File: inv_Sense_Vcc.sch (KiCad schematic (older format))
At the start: 7 parts, among them U1 ATtiny44-20SSU

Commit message: Rename to Sailor Hat
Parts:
- U1: symbol MCU_Microchip_ATtiny:ATtiny44-20SSU -> sailor-hat-rescue:ATtiny44-20SSU-MCU_Microchip_ATtiny
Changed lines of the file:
@@
-EESchema Schematic File Version 5
-LIBS:pi-supercap-ups-cache
+EESchema Schematic File Version 4
 EELAYER 30 0
 EELAYER END
@@
 Comment3 ""
 Comment4 ""
-Comment5 ""
-Comment6 ""
-Comment7 ""
-Comment8 ""
-Comment9 ""
 $EndDescr
 $Comp
@@
 	4850 2900 3800 2900
 $Comp
-L MCU_Microchip_ATtiny:ATtiny44-20SSU U1
+L sailor-hat-rescue:ATtiny44-20SSU-MCU_Microchip_ATtiny U1
 U 1 1 5D62E779
 P 3800 4500
+AR Path="/5D62E779" Ref="U1"  Part="1"
+AR Path="/5C33FF90/5D62E779" Ref="U1"  Part="1"
 F 0 "U1" H 3271 4546 50  0000 R CNN
 F 1 "ATtiny44-20SSU" H 3271 4455 50  0000 R CNN

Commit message: Update MCU to ATtiny841
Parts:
- U1: value ATtiny44-20SSU -> ATtiny841-SSU; symbol sailor-hat-rescue:ATtiny44-20SSU-MCU_Microchip_ATtiny -> MCU_Microchip_ATtiny:ATtiny841-SSU
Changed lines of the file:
@@
 	4850 2900 3800 2900
 $Comp
-L sailor-hat-rescue:ATtiny44-20SSU-MCU_Microchip_ATtiny U1
+L MCU_Microchip_ATtiny:ATtiny841-SSU U1
 U 1 1 5D62E779
 P 3800 4500
@@
 AR Path="/5C33FF90/5D62E779" Ref="U1"  Part="1"
 F 0 "U1" H 3271 4546 50  0000 R CNN
-F 1 "ATtiny44-20SSU" H 3271 4455 50  0000 R CNN
+F 1 "ATtiny841-SSU" H 3271 4455 50  0000 R CNN
 F 2 "Package_SO:SOIC-14_3.9x8.7mm_P1.27mm" H 3800 4500 50  0001 C CIN
 F 3 "http://ww1.microchip.com/downloads/en/DeviceDoc/doc8006.pdf" H 3800 4500 50  0001 C CNN

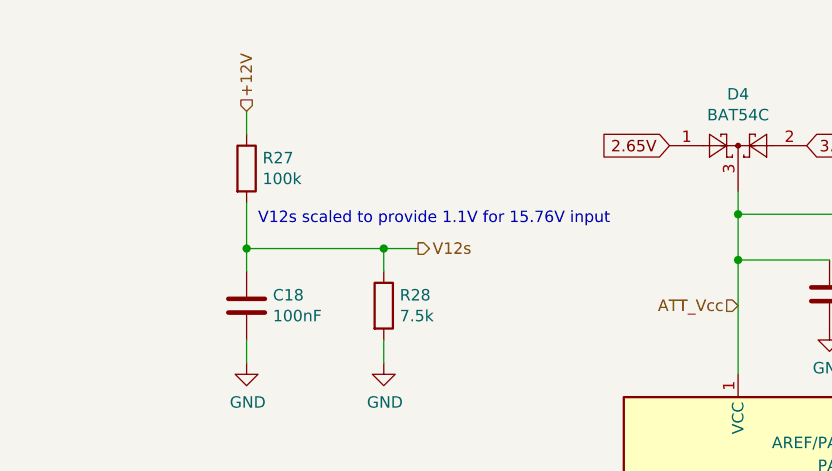
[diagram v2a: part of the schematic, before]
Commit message: Implement better current limiting
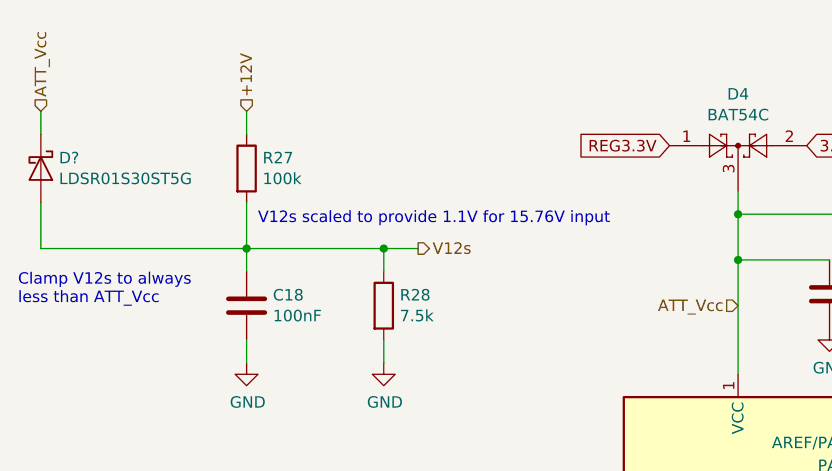
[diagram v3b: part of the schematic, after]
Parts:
- added D?: LDSR01S30ST5G, Diode_SMD:D_0603_1608Metric, symbol Device:D_Schottky
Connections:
- net ATT_Vcc: now also D?.1 (K)
- net V12s: now also D?.2 (A)
- net 2.65V renamed REG3.3V
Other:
- note added: "Clamp V12s to always\nless than ATT_Vcc"
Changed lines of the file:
@@
 $Descr A4 11693 8268
 encoding utf-8
-Sheet 4 7
+Sheet 4 6
 Title ""
 Date ""
@@
 $EndComp
 Text GLabel 3500 2600 0    50   Input ~ 0
-2.65V
+REG3.3V
 Wire Wire Line
 	5500 2900 4850 2900
@@
 Text Notes 1700 2950 0    50   ~ 0
 V12s scaled to provide 1.1V for 15.76V input
+Text HLabel 750  2450 1    50   Input ~ 0
+ATT_Vcc
+Wire Wire Line
+	750  2550 750  2450
+Wire Wire Line
+	750  2850 750  3050
+$Comp
+L Device:D_Schottky D?
+U 1 1 5E237065
+P 750 2700
+F 0 "D?" V 704 2779 50  0000 L CNN
+F 1 "LDSR01S30ST5G" V 795 2779 50  0000 L CNN
+F 2 "Diode_SMD:D_0603_1608Metric" H 750 2700 50  0001 C CNN
+F 3 "~" H 750 2700 50  0001 C CNN
+	1    750  2700
+	0    1    1    0
+$EndComp
+Wire Wire Line
+	750  3050 1650 3050
+Text Notes 650  3300 0    50   ~ 0
+Clamp V12s to always\nless than ATT_Vcc
 $EndSCHEMATC

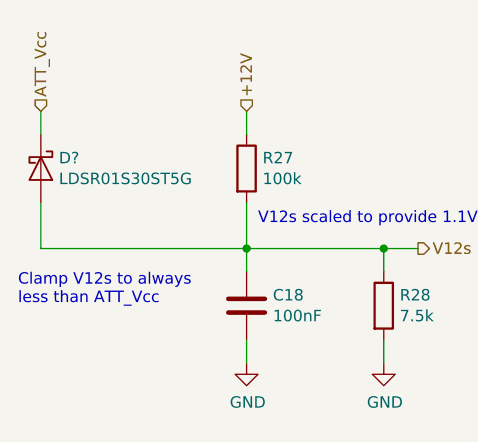
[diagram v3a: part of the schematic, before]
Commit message: Annotate and tweak power flags
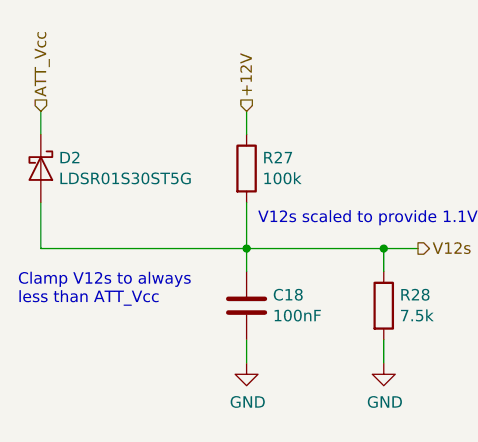
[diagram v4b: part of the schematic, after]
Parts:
- gave numbers to parts that had none: 1
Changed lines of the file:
@@
 	750  2850 750  3050
 $Comp
-L Device:D_Schottky D?
+L Device:D_Schottky D2
 U 1 1 5E237065
 P 750 2700
-F 0 "D?" V 704 2779 50  0000 L CNN
+F 0 "D2" V 704 2779 50  0000 L CNN
 F 1 "LDSR01S30ST5G" V 795 2779 50  0000 L CNN
 F 2 "Diode_SMD:D_0603_1608Metric" H 750 2700 50  0001 C CNN

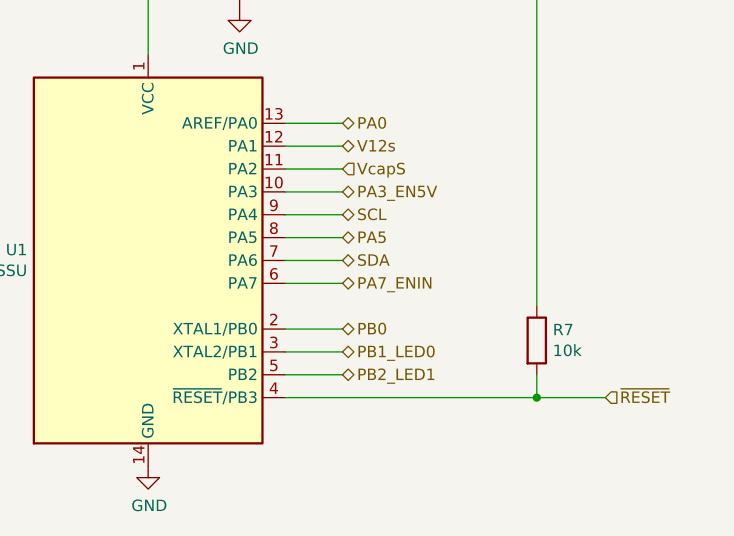
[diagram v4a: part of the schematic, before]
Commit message: Update licence, tweaks to footprints and ERC
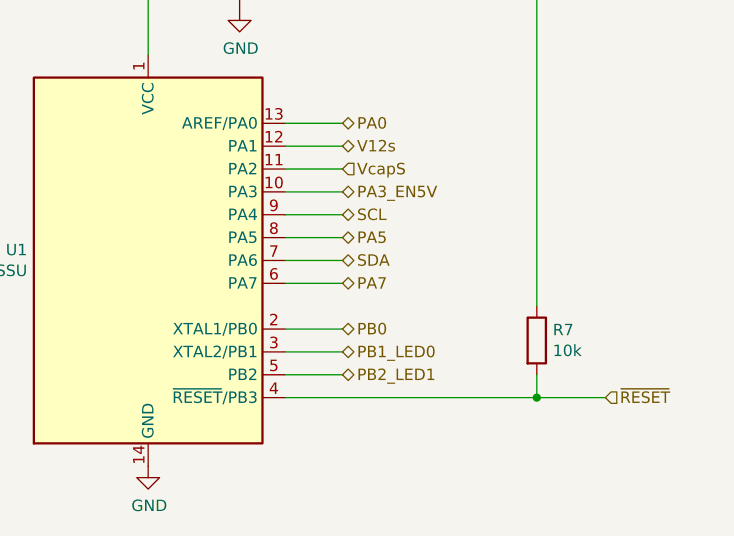
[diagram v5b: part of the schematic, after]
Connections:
- net PA7_ENIN renamed PA7
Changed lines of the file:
@@
 $Descr A4 11693 8268
 encoding utf-8
-Sheet 4 6
+Sheet 4 7
 Title ""
 Date ""
@@
 PA5
 Text HLabel 4650 4600 2    50   BiDi ~ 0
-PA7_ENIN
+PA7
 Text HLabel 4650 4200 2    50   BiDi ~ 0
 PA3_EN5V

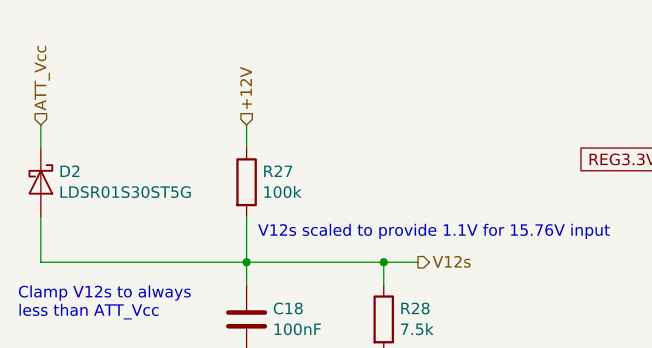
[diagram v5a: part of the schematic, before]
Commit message: Update the README, add a new rendered image of the board
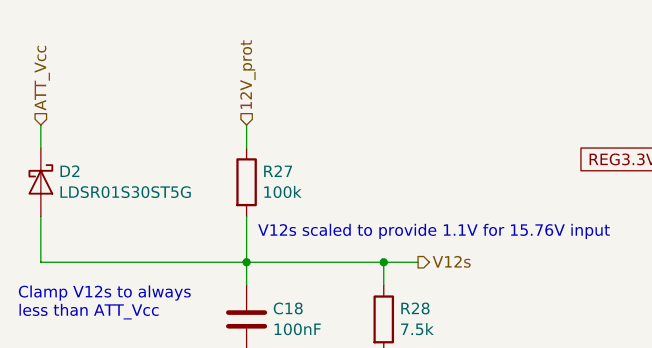
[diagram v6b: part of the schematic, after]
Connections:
- net +12V renamed 12V_prot
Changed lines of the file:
@@
 Connection ~ 1650 3050
 Text HLabel 1650 2450 1    50   Input ~ 0
-+12V
+12V_prot
 Wire Wire Line
 	1650 2450 1650 2550

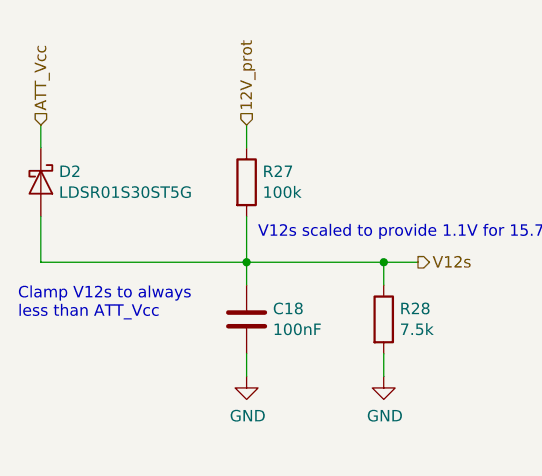
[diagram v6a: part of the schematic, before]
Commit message: Fix diode footprint
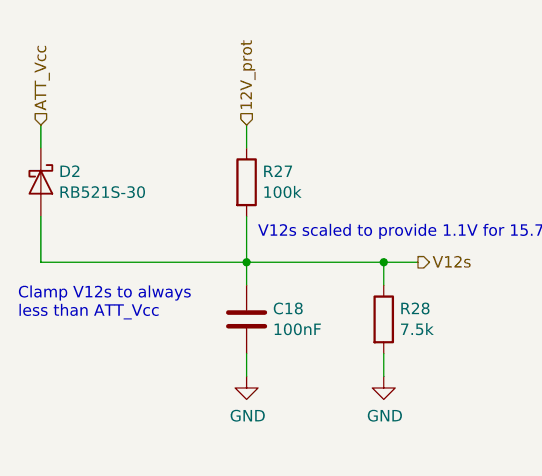
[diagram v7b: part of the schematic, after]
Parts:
- D2: value LDSR01S30ST5G -> RB521S-30; footprint Diode_SMD:D_0603_1608Metric -> Diode_SMD:D_SOD-523
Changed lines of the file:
@@
 P 750 2700
 F 0 "D2" V 704 2779 50  0000 L CNN
-F 1 "LDSR01S30ST5G" V 795 2779 50  0000 L CNN
-F 2 "Diode_SMD:D_0603_1608Metric" H 750 2700 50  0001 C CNN
+F 1 "RB521S-30" V 795 2779 50  0000 L CNN
+F 2 "Diode_SMD:D_SOD-523" H 750 2700 50  0001 C CNN
 F 3 "~" H 750 2700 50  0001 C CNN
 	1    750  2700

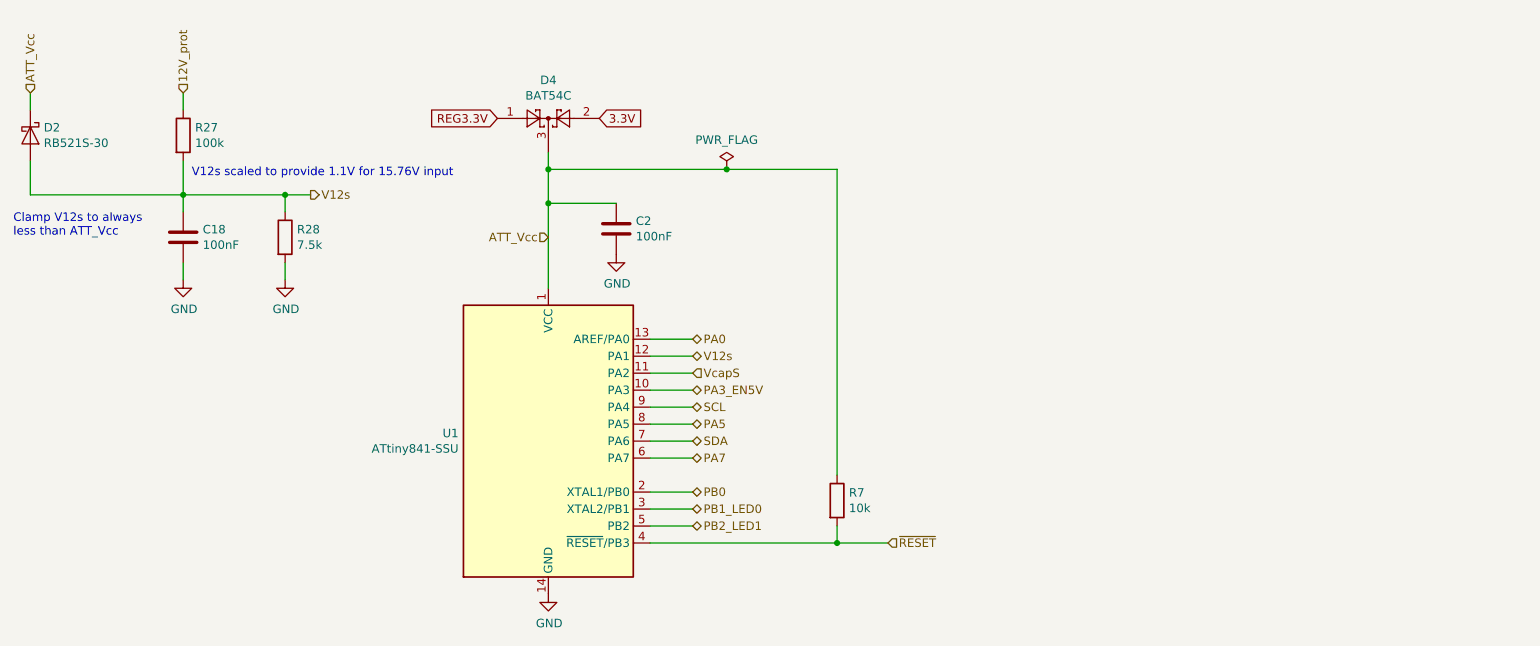
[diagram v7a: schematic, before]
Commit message: Add a voltage divider for indicating HW version
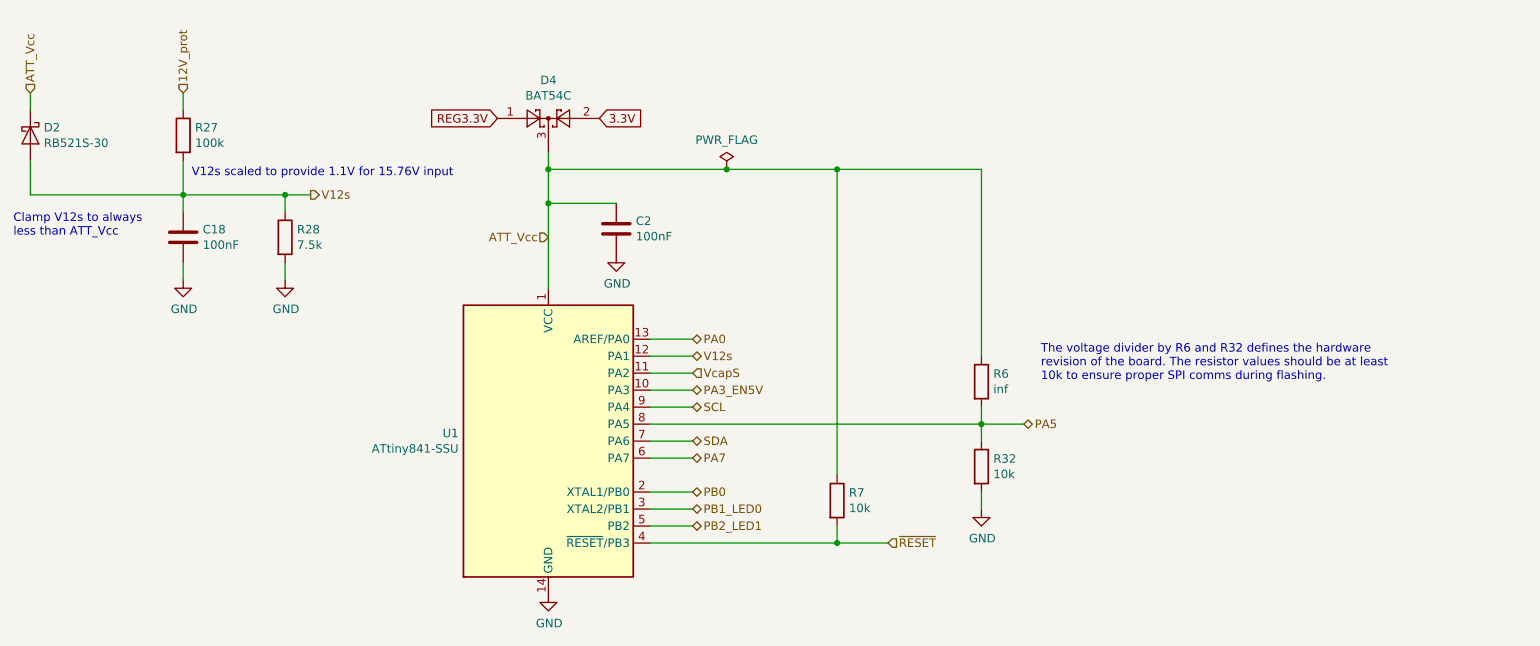
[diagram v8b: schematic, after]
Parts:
- added R32: 10k, Resistor_SMD:R_0603_1608Metric_Pad1.05x0.95mm_HandSolder, symbol Device:R
- added R6: inf, Resistor_SMD:R_0603_1608Metric_Pad1.05x0.95mm_HandSolder, symbol Device:R
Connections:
- net ATT_Vcc: now also R6.1
- net GND: now also R32.2
- net PA5: now also R32.1, R6.2
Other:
- note added: "The voltage divider by R6 and R32 defines the hardware\nrevision of the board. The resistor values should be at least\n10k to ensure proper SPI comms during flashing."
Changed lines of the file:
@@
 Text HLabel 4650 4300 2    50   BiDi ~ 0
 SCL
-Text HLabel 4650 4400 2    50   BiDi ~ 0
+Text HLabel 6600 4400 2    50   BiDi ~ 0
 PA5
 Text HLabel 4650 4600 2    50   BiDi ~ 0
@@
 Wire Wire Line
 	4650 4300 4400 4300
-Wire Wire Line
-	4400 4400 4650 4400
 Wire Wire Line
 	4650 4500 4400 4500
@@
 Text Notes 650  3300 0    50   ~ 0
 Clamp V12s to always\nless than ATT_Vcc
+$Comp
+L Device:R R32
+U 1 1 5E5DE7D1
+P 6350 4650
+F 0 "R32" H 6420 4696 50  0000 L CNN
+F 1 "10k" H 6420 4605 50  0000 L CNN
+F 2 "Resistor_SMD:R_0603_1608Metric_Pad1.05x0.95mm_HandSolder" V 6280 4650 50  0001 C CNN
+F 3 "~" H 6350 4650 50  0001 C CNN
+	1    6350 4650
+	1    0    0    -1
+$EndComp
+$Comp
+L Device:R R6
+U 1 1 5E5DFCB9
+P 6350 4150
+F 0 "R6" H 6420 4196 50  0000 L CNN
+F 1 "inf" H 6420 4105 50  0000 L CNN
+F 2 "Resistor_SMD:R_0603_1608Metric_Pad1.05x0.95mm_HandSolder" V 6280 4150 50  0001 C CNN
+F 3 "~" H 6350 4150 50  0001 C CNN
+	1    6350 4150
+	1    0    0    -1
+$EndComp
+Wire Wire Line
+	6350 4400 6350 4500
+Wire Wire Line
+	4400 4400 6350 4400
+Wire Wire Line
+	6350 4400 6350 4300
+Connection ~ 6350 4400
+Wire Wire Line
+	6350 4400 6600 4400
+Wire Wire Line
+	5500 2900 6350 2900
+Wire Wire Line
+	6350 2900 6350 4000
+Connection ~ 5500 2900
+$Comp
+L power:GND #PWR?
+U 1 1 5E5E1E1A
+P 6350 4900
+AR Path="/5E5E1E1A" Ref="#PWR?"  Part="1"
+AR Path="/5C33FF90/5E5E1E1A" Ref="#PWR056"  Part="1"
+F 0 "#PWR056" H 6350 4650 50  0001 C CNN
+F 1 "GND" H 6355 4727 50  0000 C CNN
+F 2 "" H 6350 4900 50  0001 C CNN
+F 3 "" H 6350 4900 50  0001 C CNN
+	1    6350 4900
+	1    0    0    -1
+$EndComp
+Wire Wire Line
+	6350 4900 6350 4800
+Text Notes 6700 4150 0    50   ~ 0
+The voltage divider by R6 and R32 defines the hardware\nrevision of the board. The resistor values should be at least\n10k to ensure proper SPI comms during flashing.
 $EndSCHEMATC
